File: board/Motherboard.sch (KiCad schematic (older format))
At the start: 0 parts

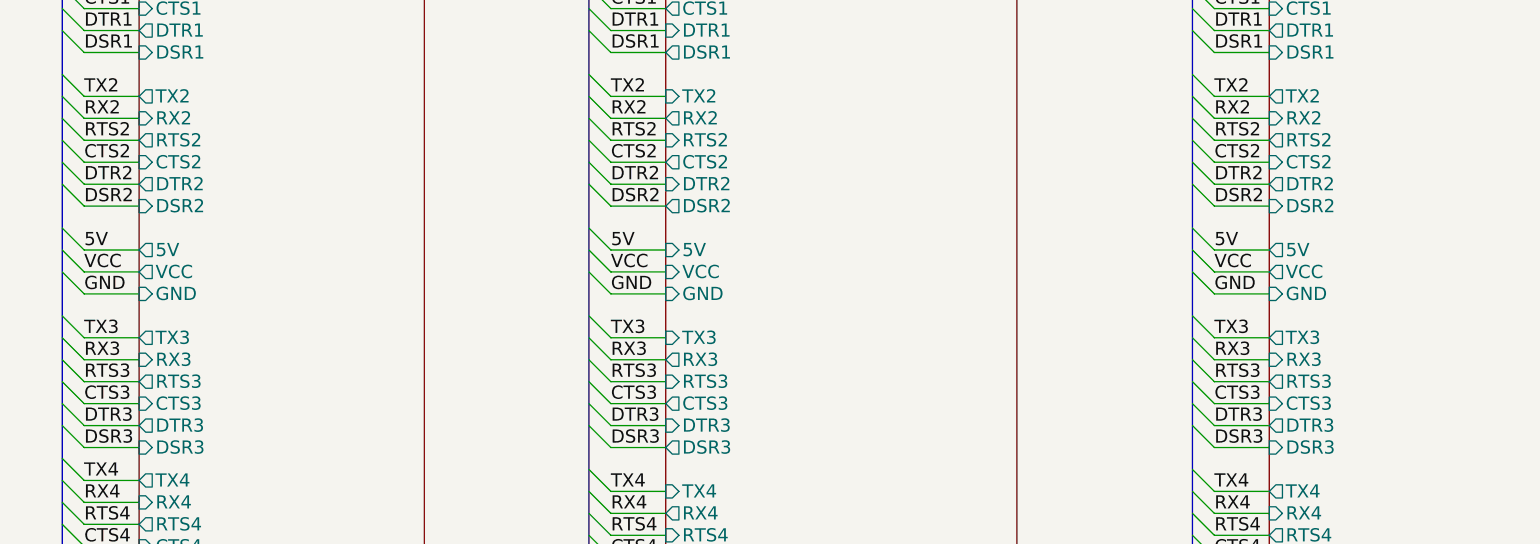
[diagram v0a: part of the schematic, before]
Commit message: Fixed power pin and port names to include voltages
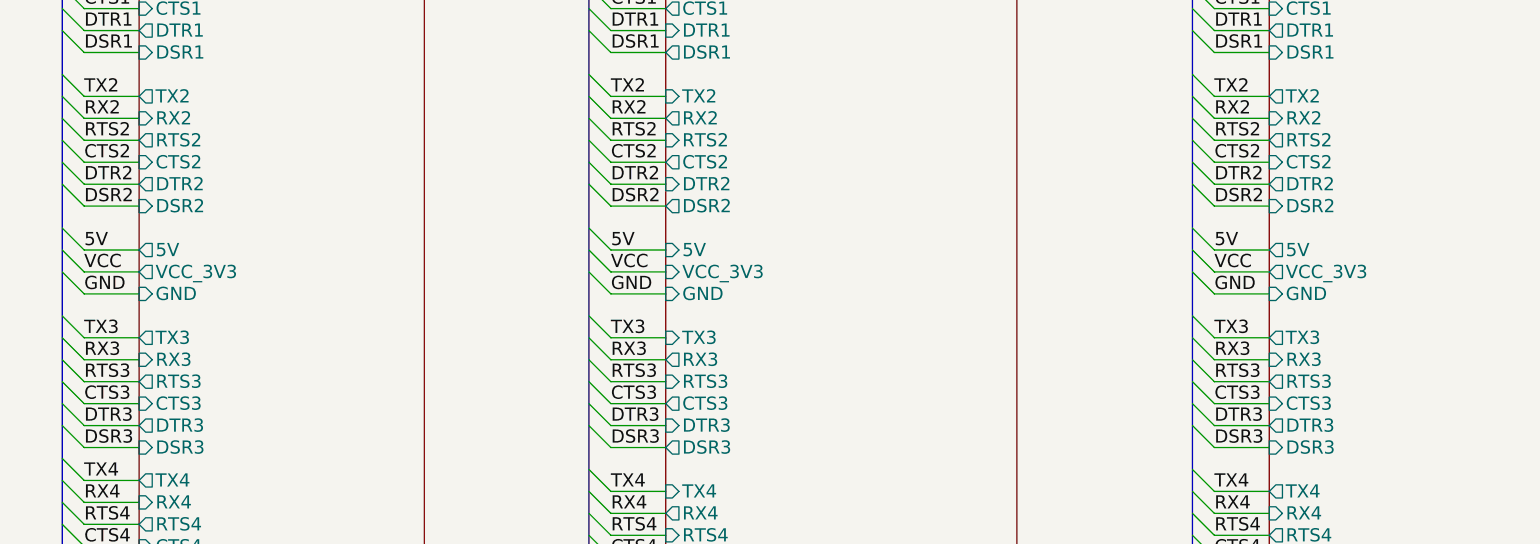
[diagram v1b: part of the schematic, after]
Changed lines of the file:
@@
 F14 "DSR1" I L 2750 2700 60
 F15 "5V" O L 2750 3600 60
-F16 "VCC" O L 2750 3700 60
+F16 "VCC_3V3" O L 2750 3700 60
 F17 "TX2" O L 2750 2900 60
 F18 "CTS2" I L 2750 3200 60
@@
 F38 "5V" O L 7900 3600 60
 F39 "GND" I L 7900 3800 60
-F40 "VCC" O L 7900 3700 60
+F40 "VCC_3V3" O L 7900 3700 60
 F41 "SDA" B L 7900 6100 60
 F42 "SCL" B L 7900 6200 60
@@
 F1 "Serial Expansion Motherboard.sch" 50
 F2 "5V" I L 5150 3600 60
-F3 "VCC" I L 5150 3700 60
+F3 "VCC_3V3" I L 5150 3700 60
 F4 "GND" I L 5150 3800 60
 F5 "TX0" I L 5150 1500 60
